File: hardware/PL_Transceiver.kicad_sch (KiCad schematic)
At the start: 4 parts, among them U2 xc7z020clg400

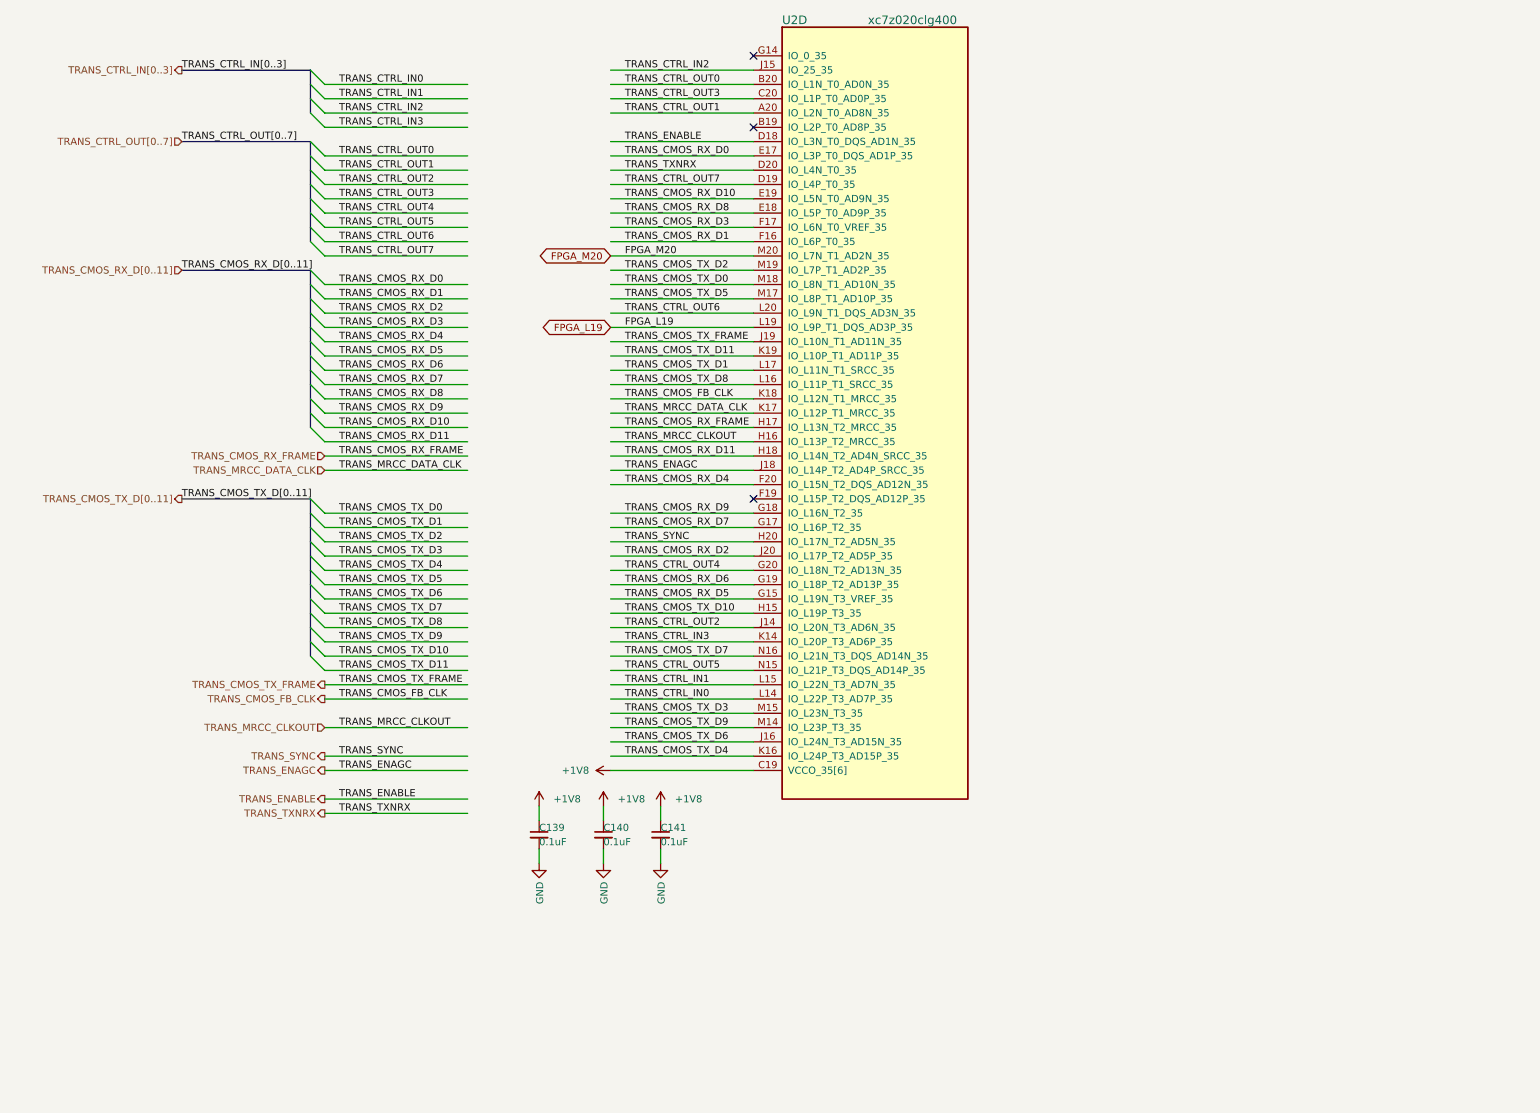
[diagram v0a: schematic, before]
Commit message: add sdio level shift ciruit
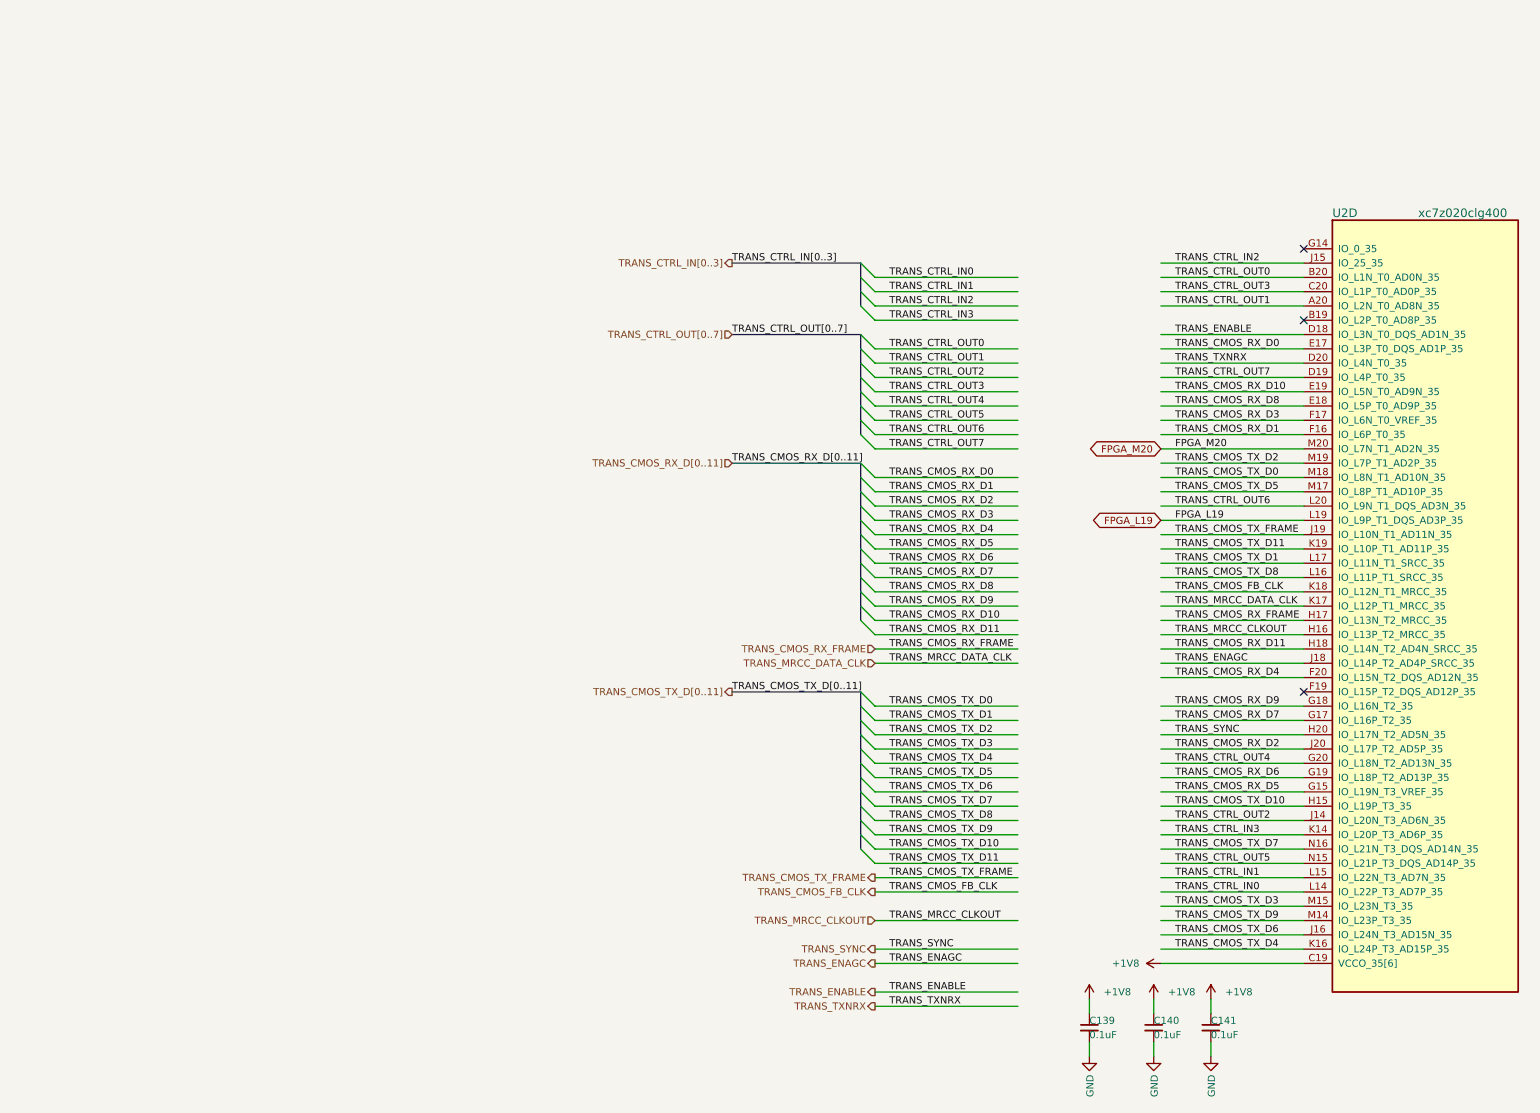
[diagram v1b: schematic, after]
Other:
- moved on the sheet: C139, C140, C141, U2D
